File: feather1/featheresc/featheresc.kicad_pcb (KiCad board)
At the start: 2 copper layers, 121 x 55 mm, 24 parts, among them J1 VIN_GND, J2 VIN_POS, J3 PHASE2, J4 PHASE1, J5 PHASE2, J6 PHASE1, J7 interconnect1, J8 interconnect2, Q1 NCEP40T20ALL, Q2 NCEP40T20ALL, Q3 NCEP40T20ALL, Q4 NCEP40T20ALL, Q5 NCEP40T20ALL, Q6 NCEP40T20ALL, Q7 NCEP40T20ALL, Q8 NCEP40T20ALL

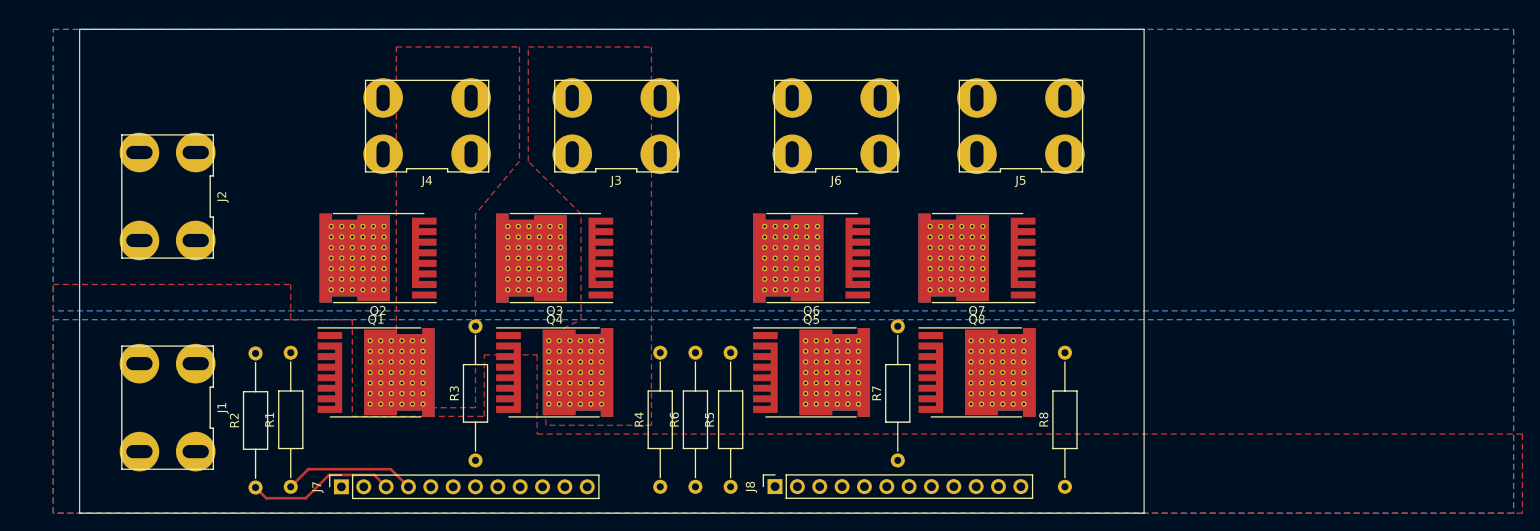
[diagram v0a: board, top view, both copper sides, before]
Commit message: Feather ESC power board
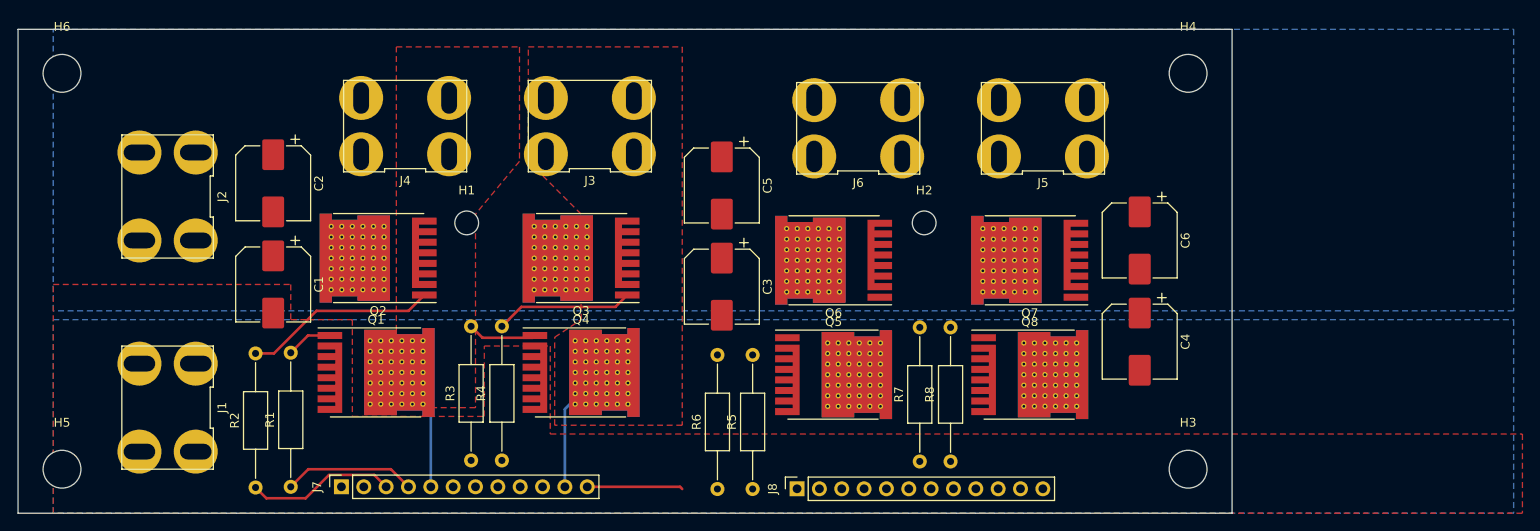
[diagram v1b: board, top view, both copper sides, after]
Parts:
- added C1: 100uF 50V, Capacitor_SMD:CP_Elec_8x10, F.Cu at (104.0, 72.0)
- added C2: 100uF 50V, Capacitor_SMD:CP_Elec_8x10, F.Cu at (104.0, 60.5)
- added C3: 100uF 50V, Capacitor_SMD:CP_Elec_8x10, F.Cu at (155.0, 72.2)
- added C4: 100uF 50V, Capacitor_SMD:CP_Elec_8x10, F.Cu at (202.5, 78.5)
- added C5: 100uF 50V, Capacitor_SMD:CP_Elec_8x10, F.Cu at (155.0, 60.8)
- added C6: 100uF 50V, Capacitor_SMD:CP_Elec_8x10, F.Cu at (202.5, 67.0)
- added H1: Interconnect M2.5, MountingHole:MountingHole_2.7mm_M2.5, F.Cu at (126.0, 65.0)
- added H2: Interconnect M2.5, MountingHole:MountingHole_2.7mm_M2.5, F.Cu at (178.0, 65.0)
- added H3: Cornerhole M4, MountingHole:MountingHole_4.3mm_M4, F.Cu at (208.0, 93.0)
- added H4: Cornerhole M4, MountingHole:MountingHole_4.3mm_M4, F.Cu at (208.0, 48.0)
- added H5: Cornerhole M4, MountingHole:MountingHole_4.3mm_M4, F.Cu at (80.0, 93.0)
- added H6: Cornerhole M4, MountingHole:MountingHole_4.3mm_M4, F.Cu at (80.0, 48.0)
- moved R4 18.2 mm to (130.0, 92.0)
- moved R8 13.3 mm to (181.0, 92.1)
- moved Q7 6.01 mm to (190.0, 69.2)
- moved Q8 6.01 mm to (190.0, 82.2)
- moved J3 3.00 mm to (140.0, 54.0)
- moved Q3 3.00 mm to (139.0, 69.0)
- moved Q4 3.00 mm to (139.0, 82.0)
- moved J5 2.51 mm to (191.5, 54.2)
- moved J6 2.51 mm to (170.5, 54.2)
- moved J8 2.51 mm to (163.6, 95.2)
- moved Q5 2.51 mm to (167.7, 82.2)
- moved Q6 2.51 mm to (167.7, 69.2)
- moved R5 2.51 mm to (158.5, 95.2)
- moved R6 2.51 mm to (154.5, 95.2)
- moved R7 2.50 mm to (177.5, 92.1)
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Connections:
- J7 pad 12: /GATE2H1 -> unconnected-(J7-Pad12)
- J7 pad 8: unconnected-(J7-Pad8) -> /GATE2H1
- J8 pad 12: /GATE2H2 -> unconnected-(J8-Pad12)
- J8 pad 6: unconnected-(J8-Pad6) -> /GATE2L2
- J8 pad 7: /GATE2L2 -> /GATE2H2
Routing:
- net Net-(Q2-Pad1): track 0.00 -> 21.9 mm
- net Net-(Q3-Pad1): track 0.00 -> 15.7 mm
- net unconnected-(J7-Pad12): track 0.00 -> 10.9 mm
- net /PHASE11: track 0.00 -> 9.77 mm
- net /PHASE21: track 0.00 -> 9.64 mm
- net Net-(Q4-Pad1): track 0.00 -> 7.90 mm
- net Net-(Q1-Pad1): track 0.00 -> 5.26 mm
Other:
- board size 121 x 55 mm -> 138 x 55 mm
